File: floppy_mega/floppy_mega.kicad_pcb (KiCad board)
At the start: 2 copper layers, 99.1 x 53.3 mm, 37 parts, among them J1 POWER, J10 MIDI IN, J11 MIDI_OUT, J2 ANALOG, J3 ANALOG, J4 DIGITAL, J5 COMMS, J6 PWM, J7 PWM, J8 MIDI IN, J9 POWER, U1 6N138

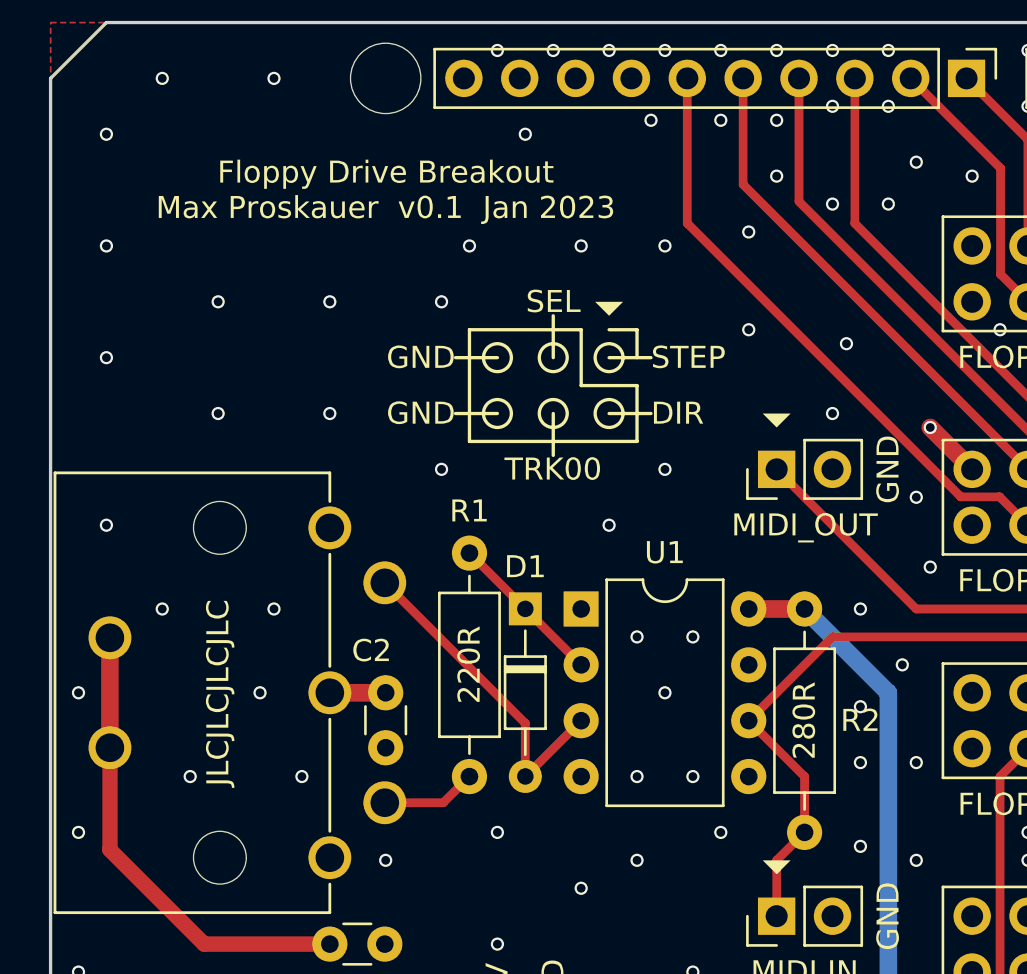
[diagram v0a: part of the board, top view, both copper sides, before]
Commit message: Add github link to breakout board
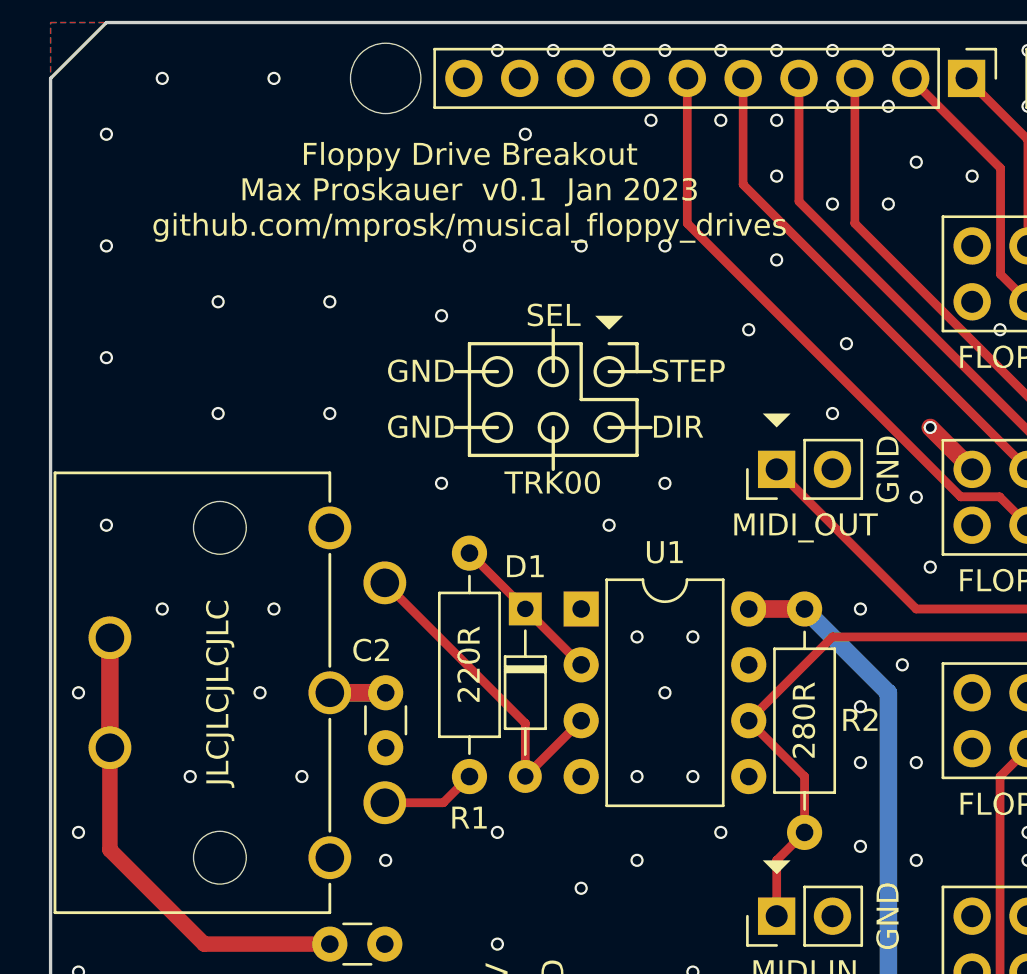
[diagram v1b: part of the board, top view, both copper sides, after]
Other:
- board text added: "Floppy Drive Breakout Max Proskauer v0.1 Jan 2023 github.com/mprosk/musical_floppy_drives"
- board text removed: "Floppy Drive Breakout Max Proskauer v0.1 Jan 2023"
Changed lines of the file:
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@@
     (property "Sheetname" "")
     (attr through_hole)
-    (fp_text reference "R1" (at -1.905 0 180) (layer "F.SilkS")
+    (fp_text reference "R1" (at 12.065 0 180) (layer "F.SilkS")
       (effects (font (size 1 1) (thickness 0.15)))
     )
@@
       (xy 137.033 106.426)
     ) (layer "F.SilkS") (width 0) (fill solid))
-  (gr_line (start 126.238 83.566) (end 126.238 81.661) (layer "F.SilkS") (width 0.15))
-  (gr_circle (center 126.238 86.106) (end 126.873 86.106) (layer "F.SilkS") (width 0.15) (fill none))
-  (gr_line (start 130.048 82.296) (end 130.048 83.566) (layer "F.SilkS") (width 0.15))
+  (gr_line (start 126.238 84.201) (end 126.238 82.296) (layer "F.SilkS") (width 0.15))
+  (gr_circle (center 126.238 86.741) (end 126.873 86.741) (layer "F.SilkS") (width 0.15) (fill none))
+  (gr_line (start 130.048 82.931) (end 130.048 84.201) (layer "F.SilkS") (width 0.15))
   (gr_poly
     (pts
@@
       (xy 151.003 75.946)
     ) (layer "F.SilkS") (width 0) (fill solid))
-  (gr_line (start 128.778 86.106) (end 130.683 86.106) (layer "F.SilkS") (width 0.15))
-  (gr_line (start 122.428 87.376) (end 130.048 87.376) (layer "F.SilkS") (width 0.15))
+  (gr_line (start 128.778 86.741) (end 130.683 86.741) (layer "F.SilkS") (width 0.15))
+  (gr_line (start 122.428 88.011) (end 130.048 88.011) (layer "F.SilkS") (width 0.15))
   (gr_poly
     (pts
@@
   (gr_poly
     (pts
-      (xy 128.778 81.661)
-      (xy 128.143 81.026)
-      (xy 129.413 81.026)
+      (xy 128.778 82.296)
+      (xy 128.143 81.661)
+      (xy 129.413 81.661)
     ) (layer "F.SilkS") (width 0) (fill solid))
   (gr_poly
@@
       (xy 192.913 106.426)
     ) (layer "F.SilkS") (width 0) (fill solid))
-  (gr_line (start 130.048 87.376) (end 130.048 84.836) (layer "F.SilkS") (width 0.15))
+  (gr_line (start 130.048 88.011) (end 130.048 85.471) (layer "F.SilkS") (width 0.15))
   (gr_line (start 182.118 73.406) (end 182.118 72.771) (layer "F.SilkS") (width 0.15))
   (gr_poly
@@
       (xy 192.913 75.946)
     ) (layer "F.SilkS") (width 0) (fill solid))
-  (gr_circle (center 128.778 83.566) (end 129.413 83.566) (layer "F.SilkS") (width 0.15) (fill none))
+  (gr_circle (center 128.778 84.201) (end 129.413 84.201) (layer "F.SilkS") (width 0.15) (fill none))
   (gr_poly
     (pts
@@
     ) (layer "F.SilkS") (width 0) (fill solid))
   (gr_line (start 189.738 73.406) (end 188.468 73.406) (layer "F.SilkS") (width 0.15))
-  (gr_line (start 128.778 82.296) (end 130.048 82.296) (layer "F.SilkS") (width 0.15))
-  (gr_circle (center 123.698 86.106) (end 124.333 86.106) (layer "F.SilkS") (width 0.15) (fill none))
+  (gr_line (start 128.778 82.931) (end 130.048 82.931) (layer "F.SilkS") (width 0.15))
+  (gr_circle (center 123.698 86.741) (end 124.333 86.741) (layer "F.SilkS") (width 0.15) (fill none))
   (gr_poly
     (pts
@@
       (xy 164.973 75.946)
     ) (layer "F.SilkS") (width 0) (fill solid))
-  (gr_line (start 127.508 82.296) (end 122.428 82.296) (layer "F.SilkS") (width 0.15))
+  (gr_line (start 127.508 82.931) (end 122.428 82.931) (layer "F.SilkS") (width 0.15))
   (gr_poly
     (pts
@@
       (xy 164.973 86.106)
     ) (layer "F.SilkS") (width 0) (fill solid))
-  (gr_line (start 123.698 83.566) (end 121.793 83.566) (layer "F.SilkS") (width 0.15))
+  (gr_line (start 123.698 84.201) (end 121.793 84.201) (layer "F.SilkS") (width 0.15))
   (gr_line (start 183.388 73.406) (end 182.118 73.406) (layer "F.SilkS") (width 0.15))
   (gr_poly
@@
       (xy 164.973 96.266)
     ) (layer "F.SilkS") (width 0) (fill solid))
-  (gr_circle (center 128.778 86.106) (end 129.413 86.106) (layer "F.SilkS") (width 0.15) (fill none))
+  (gr_circle (center 128.778 86.741) (end 129.413 86.741) (layer "F.SilkS") (width 0.15) (fill none))
   (gr_line (start 189.738 72.771) (end 189.738 73.406) (layer "F.SilkS") (width 0.15))
-  (gr_line (start 122.428 82.296) (end 122.428 87.376) (layer "F.SilkS") (width 0.15))
-  (gr_circle (center 126.238 83.566) (end 126.873 83.566) (layer "F.SilkS") (width 0.15) (fill none))
+  (gr_line (start 122.428 82.931) (end 122.428 88.011) (layer "F.SilkS") (width 0.15))
+  (gr_circle (center 126.238 84.201) (end 126.873 84.201) (layer "F.SilkS") (width 0.15) (fill none))
   (gr_poly
     (pts
@@
       (xy 164.973 106.426)
     ) (layer "F.SilkS") (width 0) (fill solid))
-  (gr_line (start 128.778 83.566) (end 130.683 83.566) (layer "F.SilkS") (width 0.15))
-  (gr_circle (center 123.698 83.566) (end 124.333 83.566) (layer "F.SilkS") (width 0.15) (fill none))
-  (gr_line (start 126.238 86.106) (end 126.238 88.011) (layer "F.SilkS") (width 0.15))
+  (gr_line (start 128.778 84.201) (end 130.683 84.201) (layer "F.SilkS") (width 0.15))
+  (gr_circle (center 123.698 84.201) (end 124.333 84.201) (layer "F.SilkS") (width 0.15) (fill none))
+  (gr_line (start 126.238 86.741) (end 126.238 88.646) (layer "F.SilkS") (width 0.15))
   (gr_poly
     (pts
@@
       (xy 151.003 96.266)
     ) (layer "F.SilkS") (width 0) (fill solid))
-  (gr_line (start 121.793 86.106) (end 123.698 86.106) (layer "F.SilkS") (width 0.15))
-  (gr_line (start 127.508 84.836) (end 130.048 84.836) (layer "F.SilkS") (width 0.15))
-  (gr_line (start 127.508 82.296) (end 127.508 84.836) (layer "F.SilkS") (width 0.15))
+  (gr_line (start 121.793 86.741) (end 123.698 86.741) (layer "F.SilkS") (width 0.15))
+  (gr_line (start 127.508 85.471) (end 130.048 85.471) (layer "F.SilkS") (width 0.15))
+  (gr_line (start 127.508 82.931) (end 127.508 85.471) (layer "F.SilkS") (width 0.15))
   (gr_line locked (start 165.735 97.536) (end 165.735 89.916) (layer "Dwgs.User") (width 0.15))
   (gr_line (start 125.603 73.406) (end 125.603 78.486) (layer "Dwgs.User") (width 0.15))
@@
     (effects (font (size 1 1) (thickness 0.15)))
   )
-  (gr_text "TRK00" (at 126.238 88.646) (layer "F.SilkS")
+  (gr_text "TRK00" (at 126.238 89.281) (layer "F.SilkS")
     (effects (font (size 1 1) (thickness 0.15)))
   )
-  (gr_text "Floppy Drive Breakout\nMax Proskauer  v0.1  Jan 2023" (at 118.618 75.946) (layer "F.SilkS")
+  (gr_text "Floppy Drive Breakout\nMax Proskauer  v0.1  Jan 2023\ngithub.com/mprosk/musical_floppy_drives" (at 122.428 75.946) (layer "F.SilkS")
     (effects (font (size 1 1) (thickness 0.15)))
   )
-  (gr_text "GND" (at 121.793 86.106) (layer "F.SilkS")
+  (gr_text "GND" (at 121.793 86.741) (layer "F.SilkS")
     (effects (font (size 1 1) (thickness 0.15)) (justify right))
   )
-  (gr_text "DIR" (at 130.683 86.106) (layer "F.SilkS")
+  (gr_text "DIR" (at 130.683 86.741) (layer "F.SilkS")
     (effects (font (size 1 1) (thickness 0.15)) (justify left))
   )
@@
     (effects (font (size 1 1) (thickness 0.15)))
   )
-  (gr_text "STEP" (at 130.683 83.566) (layer "F.SilkS")
+  (gr_text "STEP" (at 130.683 84.201) (layer "F.SilkS")
     (effects (font (size 1 1) (thickness 0.15)) (justify left))
   )
-  (gr_text "GND" (at 121.793 83.566) (layer "F.SilkS")
+  (gr_text "GND" (at 121.793 84.201) (layer "F.SilkS")
     (effects (font (size 1 1) (thickness 0.15)) (justify right))
   )
-  (gr_text "SEL" (at 126.238 81.026) (layer "F.SilkS")
+  (gr_text "SEL" (at 126.238 81.661) (layer "F.SilkS")
     (effects (font (size 1 1) (thickness 0.15)))
   )
@@
   (via (at 147.828 120.396) (size 0.6) (drill 0.4) (layers "F.Cu" "B.Cu") (free) (net 1))
   (via (at 116.078 81.026) (size 0.6) (drill 0.4) (layers "F.Cu" "B.Cu") (free) (net 1))
-  (via (at 121.158 88.646) (size 0.6) (drill 0.4) (layers "F.Cu" "B.Cu") (free) (net 1))
+  (via (at 121.158 89.281) (size 0.6) (drill 0.4) (layers "F.Cu" "B.Cu") (free) (net 1))
   (via (at 201.168 94.996) (size 0.6) (drill 0.4) (layers "F.Cu" "B.Cu") (free) (net 1))
   (via (at 105.918 91.186) (size 0.6) (drill 0.4) (layers "F.Cu" "B.Cu") (free) (net 1))
@@
   (via (at 185.928 100.076) (size 0.6) (drill 0.4) (layers "F.Cu" "B.Cu") (free) (net 1))
   (via (at 174.498 107.696) (size 0.6) (drill 0.4) (layers "F.Cu" "B.Cu") (free) (net 1))
-  (via (at 135.128 77.851) (size 0.6) (drill 0.4) (layers "F.Cu" "B.Cu") (free) (net 1))
+  (via (at 136.398 79.121) (size 0.6) (drill 0.4) (layers "F.Cu" "B.Cu") (free) (net 1))
   (via (at 140.208 94.996) (size 0.6) (drill 0.4) (layers "F.Cu" "B.Cu") (free) (net 1))
   (via (at 157.988 69.596) (size 0.6) (drill 0.4) (layers "F.Cu" "B.Cu") (free) (net 1))
@@
   (via (at 152.908 81.026) (size 0.6) (drill 0.4) (layers "F.Cu" "B.Cu") (free) (net 1))
   (via (at 183.388 120.396) (size 0.6) (drill 0.4) (layers "F.Cu" "B.Cu") (free) (net 1))
-  (via (at 121.158 81.026) (size 0.6) (drill 0.4) (layers "F.Cu" "B.Cu") (free) (net 1))
+  (via (at 121.158 81.661) (size 0.6) (drill 0.4) (layers "F.Cu" "B.Cu") (free) (net 1))
   (via (at 188.468 82.296) (size 0.6) (drill 0.4) (layers "F.Cu" "B.Cu") (free) (net 1))
   (via (at 152.908 72.136) (size 0.6) (drill 0.4) (layers "F.Cu" "B.Cu") (free) (net 1))
@@
   (via (at 142.748 120.396) (size 0.6) (drill 0.4) (layers "F.Cu" "B.Cu") (free) (net 1))
   (via (at 151.638 119.126) (size 0.6) (drill 0.4) (layers "F.Cu" "B.Cu") (free) (net 1))
-  (via (at 131.318 88.646) (size 0.6) (drill 0.4) (layers "F.Cu" "B.Cu") (free) (net 1))
+  (via (at 131.318 89.281) (size 0.6) (drill 0.4) (layers "F.Cu" "B.Cu") (free) (net 1))
   (segment (start 123.698 117.856) (end 123.698 116.586) (width 0.8) (layer "F.Cu") (net 2))
   (segment (start 135.128 94.996) (end 137.668 94.996) (width 0.8) (layer "F.Cu") (net 2))
